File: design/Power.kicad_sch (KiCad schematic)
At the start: 43 parts, among them J5 PH_A, J6 PH_B, J7 PH_C, J8 SUPPLY, J9 GND, Q1 IRF7854, Q2 IRF7854, Q3 IRF7854, Q4 IRF7854, Q5 IRF7854, Q6 IRF7854, U5 AD8418, U6 AD8418, U7 AD8418

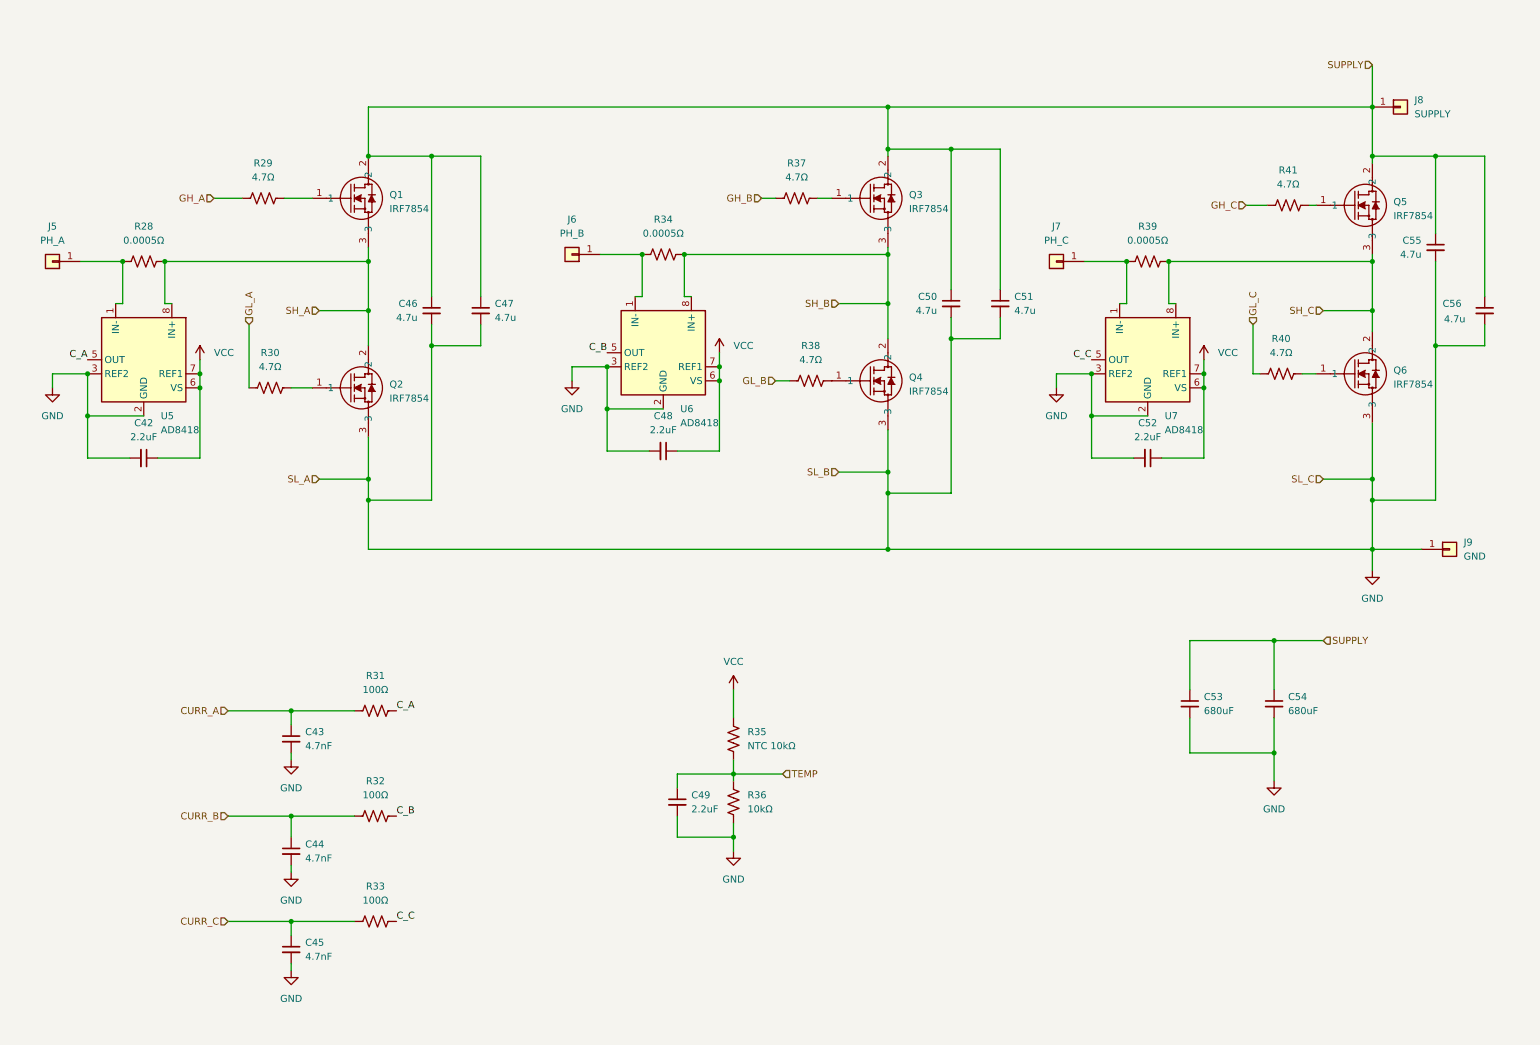
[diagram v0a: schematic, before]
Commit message: Ordenado del esquemático
- Cambios en los capacitores del oscilador
- Mejora de los esquemáticos, encapsulado la interfáz usb y los sensores del motor
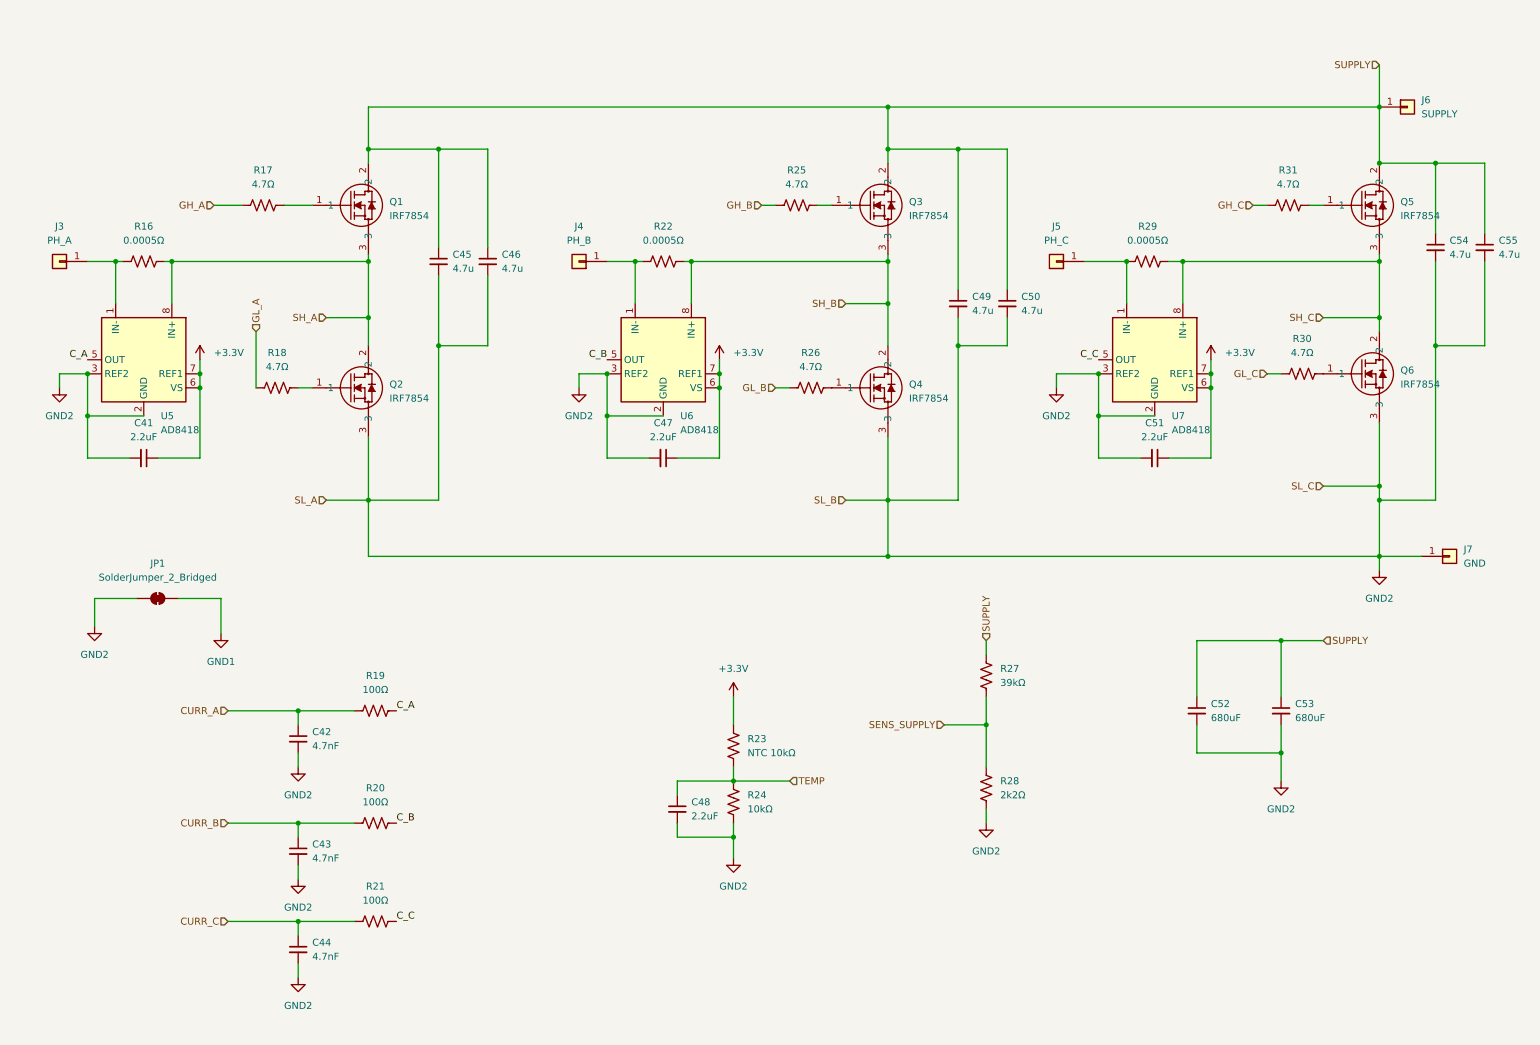
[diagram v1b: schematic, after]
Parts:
- added JP1: SolderJumper_2_Bridged, symbol Jumper:SolderJumper_2_Bridged
- added R27: 39kΩ, Resistor_SMD:R_0603_1608Metric, symbol Device:R_US
- added R28: 2k2Ω, Resistor_SMD:R_0603_1608Metric, symbol Device:R_US
- renumbered C42 to C41, C43 to C42, C44 to C43, C45 to C44, C46 to C45, C47 to C46, C48 to C47, C49 to C48, C50 to C49, C51 to C50, C52 to C51, C53 to C52, C54 to C53, C55 to C54, C56 to C55, J5 to J3, J6 to J4, J7 to J5, J8 to J6, J9 to J7, R28 to R16, R29 to R17, R30 to R18, R31 to R19, R32 to R20, R33 to R21, R34 to R22, R35 to R23, R36 to R24, R37 to R25, R38 to R26, R39 to R29, R40 to R30, R41 to R31
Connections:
- net SUPPLY: now also R27.1
- net GND renamed GND2
- net GND2: now also JP1.1 (A), R28.1
- net VCC renamed +3.3V
- new net GND1: JP1.2 (B)
- new net SENS_SUPPLY: R27.2, R28.2
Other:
- moved on the sheet: C42, C43, C44, C45, C46, C47, C48, C49, C50, C51, C52, C53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

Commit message: Pequeños cambios
Pequeños cambios, eliminado de carpeta BLDC
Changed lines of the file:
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@@
 	(hierarchical_label "SUPPLY"
 		(shape input)
-		(at 259.08 20.32 180)
+		(at 259.08 20.32 90)
 		(fields_autoplaced yes)
 		(effects
@@
 				(size 1.27 1.27)
 			)
-			(justify right)
+			(justify left)
 		)
 	)

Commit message: Pequeños cambios
Pequeños cambios en esquemático
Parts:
- renumbered R16 to R17, R17 to R18, R18 to R19, R19 to R20, R20 to R21, R21 to R22, R22 to R23, R23 to R24, R24 to R25, R25 to R26, R26 to R27, R27 to R28, R28 to R29, R29 to R30, R30 to R32
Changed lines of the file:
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@@
 		(dnp no)
 		(fields_autoplaced yes)
-		(property "Reference" "R25"
+		(property "Reference" "R26"
 			(at 153.67 39.37 90)
 			(effects
@@
 			(project "ESCX"
 				(path "/6389d757-a1bd-4c0a-9d55-6114b19cc67a/00000000-0000-0000-0000-00005ae14a7c"
-					(reference "R25")
+					(reference "R26")
 					(unit 1)
 				)
@@
 		(dnp no)
 		(fields_autoplaced yes)
-		(property "Reference" "R22"
+		(property "Reference" "R23"
 			(at 129.54 49.53 90)
 			(effects
@@
 			(project "ESCX"
 				(path "/6389d757-a1bd-4c0a-9d55-6114b19cc67a/00000000-0000-0000-0000-00005ae14a7c"
-					(reference "R22")
+					(reference "R23")
 					(unit 1)
 				)
@@
 		(dnp no)
 		(fields_autoplaced yes)
-		(property "Reference" "R26"
+		(property "Reference" "R27"
 			(at 156.21 72.39 90)
 			(effects
@@
 			(project "ESCX"
 				(path "/6389d757-a1bd-4c0a-9d55-6114b19cc67a/00000000-0000-0000-0000-00005ae14a7c"
-					(reference "R26")
+					(reference "R27")
 					(unit 1)
 				)
@@
 		(dnp no)
 		(fields_autoplaced yes)
-		(property "Reference" "#PWR056"
+		(property "Reference" "#PWR058"
 			(at 139.7 77.47 0)
 			(effects
@@
 			(project "ESCX"
 				(path "/6389d757-a1bd-4c0a-9d55-6114b19cc67a/00000000-0000-0000-0000-00005ae14a7c"
-					(reference "#PWR056")
+					(reference "#PWR058")
 					(unit 1)
 				)
@@
 		(dnp no)
 		(fields_autoplaced yes)
-		(property "Reference" "R17"
+		(property "Reference" "R18"
 			(at 57.15 39.37 90)
 			(effects
@@
 			(project "ESCX"
 				(path "/6389d757-a1bd-4c0a-9d55-6114b19cc67a/00000000-0000-0000-0000-00005ae14a7c"
-					(reference "R17")
+					(reference "R18")
 					(unit 1)
 				)
@@
 		(dnp no)
 		(fields_autoplaced yes)
-		(property "Reference" "R16"
+		(property "Reference" "R17"
 			(at 35.56 49.53 90)
 			(effects
@@
 			(project "ESCX"
 				(path "/6389d757-a1bd-4c0a-9d55-6114b19cc67a/00000000-0000-0000-0000-00005ae14a7c"
-					(reference "R16")
+					(reference "R17")
 					(unit 1)
 				)
@@
 		(dnp no)
 		(fields_autoplaced yes)
-		(property "Reference" "R18"
+		(property "Reference" "R19"
 			(at 59.69 72.39 90)
 			(effects
@@
 			(project "ESCX"
 				(path "/6389d757-a1bd-4c0a-9d55-6114b19cc67a/00000000-0000-0000-0000-00005ae14a7c"
-					(reference "R18")
+					(reference "R19")
 					(unit 1)
 				)
@@
 		(dnp no)
 		(fields_autoplaced yes)
-		(property "Reference" "#PWR051"
+		(property "Reference" "#PWR052"
 			(at 45.72 77.47 0)
 			(effects
@@
 			(project "ESCX"
 				(path "/6389d757-a1bd-4c0a-9d55-6114b19cc67a/00000000-0000-0000-0000-00005ae14a7c"
-					(reference "#PWR051")
+					(reference "#PWR052")
 					(unit 1)
 				)
@@
 		(dnp no)
 		(fields_autoplaced yes)
-		(property "Reference" "R29"
+		(property "Reference" "R30"
 			(at 217.17 49.53 90)
 			(effects
@@
 			(project "ESCX"
 				(path "/6389d757-a1bd-4c0a-9d55-6114b19cc67a/00000000-0000-0000-0000-00005ae14a7c"
-					(reference "R29")
+					(reference "R30")
 					(unit 1)
 				)
@@
 		(dnp no)
 		(fields_autoplaced yes)
-		(property "Reference" "R30"
+		(property "Reference" "R32"
 			(at 245.11 69.85 90)
 			(effects
@@
 			(project "ESCX"
 				(path "/6389d757-a1bd-4c0a-9d55-6114b19cc67a/00000000-0000-0000-0000-00005ae14a7c"
-					(reference "R30")
+					(reference "R32")
 					(unit 1)
 				)
@@
 		(dnp no)
 		(fields_autoplaced yes)
-		(property "Reference" "#PWR061"
+		(property "Reference" "#PWR063"
 			(at 228.6 77.47 0)
 			(effects
@@
 			(project "ESCX"
 				(path "/6389d757-a1bd-4c0a-9d55-6114b19cc67a/00000000-0000-0000-0000-00005ae14a7c"
-					(reference "#PWR061")
+					(reference "#PWR063")
 					(unit 1)
 				)
@@
 		(dnp no)
 		(fields_autoplaced yes)
-		(property "Reference" "#PWR63"
+		(property "Reference" "#PWR065"
 			(at 259.08 118.11 0)
 			(effects
@@
 			(project "ESCX"
 				(path "/6389d757-a1bd-4c0a-9d55-6114b19cc67a/00000000-0000-0000-0000-00005ae14a7c"
-					(reference "#PWR63")
+					(reference "#PWR065")
 					(unit 1)
 				)
@@
 		(dnp no)
 		(fields_autoplaced yes)
-		(property "Reference" "R19"
+		(property "Reference" "R20"
 			(at 77.47 130.81 90)
 			(effects
@@
 			(project "ESCX"
 				(path "/6389d757-a1bd-4c0a-9d55-6114b19cc67a/00000000-0000-0000-0000-00005ae14a7c"
-					(reference "R19")
+					(reference "R20")
 					(unit 1)
 				)
@@
 		(dnp no)
 		(fields_autoplaced yes)
-		(property "Reference" "R20"
+		(property "Reference" "R21"
 			(at 77.47 151.13 90)
 			(effects
@@
 			(project "ESCX"
 				(path "/6389d757-a1bd-4c0a-9d55-6114b19cc67a/00000000-0000-0000-0000-00005ae14a7c"
-					(reference "R20")
+					(reference "R21")
 					(unit 1)
 				)
@@
 		(dnp no)
 		(fields_autoplaced yes)
-		(property "Reference" "R21"
+		(property "Reference" "R22"
 			(at 77.47 168.91 90)
 			(effects
@@
 			(project "ESCX"
 				(path "/6389d757-a1bd-4c0a-9d55-6114b19cc67a/00000000-0000-0000-0000-00005ae14a7c"
-					(reference "R21")
+					(reference "R22")
 					(unit 1)
 				)
@@
 		(dnp no)
 		(fields_autoplaced yes)
-		(property "Reference" "#PWR057"
+		(property "Reference" "#PWR059"
 			(at 142.24 138.43 0)
 			(effects
@@
 			(project "ESCX"
 				(path "/6389d757-a1bd-4c0a-9d55-6114b19cc67a/00000000-0000-0000-0000-00005ae14a7c"
-					(reference "#PWR057")
+					(reference "#PWR059")
 					(unit 1)
 				)
@@
 		(dnp no)
 		(fields_autoplaced yes)
-		(property "Reference" "R24"
+		(property "Reference" "R25"
 			(at 144.78 152.3999 0)
 			(effects
@@
 			(project "ESCX"
 				(path "/6389d757-a1bd-4c0a-9d55-6114b19cc67a/00000000-0000-0000-0000-00005ae14a7c"
-					(reference "R24")
+					(reference "R25")
 					(unit 1)
 				)
@@
 		(dnp no)
 		(fields_autoplaced yes)
-		(property "Reference" "R23"
+		(property "Reference" "R24"
 			(at 144.78 142.2399 0)
 			(effects
@@
 			(project "ESCX"
 				(path "/6389d757-a1bd-4c0a-9d55-6114b19cc67a/00000000-0000-0000-0000-00005ae14a7c"
-					(reference "R23")
+					(reference "R24")
 					(unit 1)
 				)
@@
 		(dnp no)
 		(fields_autoplaced yes)
-		(property "Reference" "#PWR060"
+		(property "Reference" "#PWR062"
 			(at 200.66 85.09 0)
 			(effects
@@
 			(project "ESCX"
 				(path "/6389d757-a1bd-4c0a-9d55-6114b19cc67a/00000000-0000-0000-0000-00005ae14a7c"
-					(reference "#PWR060")
+					(reference "#PWR062")
 					(unit 1)
 				)
@@
 		(dnp no)
 		(fields_autoplaced yes)
-		(property "Reference" "#PWR055"
+		(property "Reference" "#PWR057"
 			(at 114.3 85.09 0)
 			(effects
@@
 			(project "ESCX"
 				(path "/6389d757-a1bd-4c0a-9d55-6114b19cc67a/00000000-0000-0000-0000-00005ae14a7c"
-					(reference "#PWR055")
+					(reference "#PWR057")
 					(unit 1)
 				)
@@
 		(dnp no)
 		(fields_autoplaced yes)
-		(property "Reference" "R28"
+		(property "Reference" "R29"
 			(at 190.5 149.8599 0)
 			(effects
@@
 			(project "ESCX"
 				(path "/6389d757-a1bd-4c0a-9d55-6114b19cc67a/00000000-0000-0000-0000-00005ae14a7c"
-					(reference "R28")
+					(reference "R29")
 					(unit 1)
 				)
@@
 		(dnp no)
 		(fields_autoplaced yes)
-		(property "Reference" "#PWR059"
+		(property "Reference" "#PWR061"
 			(at 187.96 163.83 0)
 			(effects
@@
 			(project "ESCX"
 				(path "/6389d757-a1bd-4c0a-9d55-6114b19cc67a/00000000-0000-0000-0000-00005ae14a7c"
-					(reference "#PWR059")
+					(reference "#PWR061")
 					(unit 1)
 				)
@@
 		(dnp no)
 		(fields_autoplaced yes)
-		(property "Reference" "#PWR053"
+		(property "Reference" "#PWR055"
 			(at 63.5 173.99 0)
 			(effects
@@
 			(project "ESCX"
 				(path "/6389d757-a1bd-4c0a-9d55-6114b19cc67a/00000000-0000-0000-0000-00005ae14a7c"
-					(reference "#PWR053")
+					(reference "#PWR055")
 					(unit 1)
 				)
@@
 		(dnp no)
 		(fields_autoplaced yes)
-		(property "Reference" "#PWR052"
+		(property "Reference" "#PWR054"
 			(at 63.5 153.67 0)
 			(effects
@@
 			(project "ESCX"
 				(path "/6389d757-a1bd-4c0a-9d55-6114b19cc67a/00000000-0000-0000-0000-00005ae14a7c"
-					(reference "#PWR052")
+					(reference "#PWR054")
 					(unit 1)
 				)
@@
 		(dnp no)
 		(fields_autoplaced yes)
-		(property "Reference" "R27"
+		(property "Reference" "R28"
 			(at 190.5 129.5399 0)
 			(effects
@@
 			(project "ESCX"
 				(path "/6389d757-a1bd-4c0a-9d55-6114b19cc67a/00000000-0000-0000-0000-00005ae14a7c"
-					(reference "R27")
+					(reference "R28")
 					(unit 1)
 				)
@@
 		(dnp no)
 		(fields_autoplaced yes)
-		(property "Reference" "#PWR074"
+		(property "Reference" "#PWR051"
 			(at 26.67 128.27 0)
 			(effects
@@
 			(project "ESCX"
 				(path "/6389d757-a1bd-4c0a-9d55-6114b19cc67a/00000000-0000-0000-0000-00005ae14a7c"
-					(reference "#PWR074")
+					(reference "#PWR051")
 					(unit 1)
 				)
@@
 		(dnp no)
 		(fields_autoplaced yes)
-		(property "Reference" "#PWR058"
+		(property "Reference" "#PWR060"
 			(at 142.24 170.18 0)
 			(effects
@@
 			(project "ESCX"
 				(path "/6389d757-a1bd-4c0a-9d55-6114b19cc67a/00000000-0000-0000-0000-00005ae14a7c"
-					(reference "#PWR058")
+					(reference "#PWR060")
 					(unit 1)
 				)
@@
 		(dnp no)
 		(fields_autoplaced yes)
-		(property "Reference" "#PWR054"
+		(property "Reference" "#PWR056"
 			(at 63.5 191.77 0)
 			(effects
@@
 			(project "ESCX"
 				(path "/6389d757-a1bd-4c0a-9d55-6114b19cc67a/00000000-0000-0000-0000-00005ae14a7c"
-					(reference "#PWR054")
+					(reference "#PWR056")
 					(unit 1)
 				)
@@
 		(dnp no)
 		(fields_autoplaced yes)
-		(property "Reference" "#PWR062"
+		(property "Reference" "#PWR064"
 			(at 241.3 156.21 0)
 			(effects
@@
 			(project "ESCX"
 				(path "/6389d757-a1bd-4c0a-9d55-6114b19cc67a/00000000-0000-0000-0000-00005ae14a7c"
-					(reference "#PWR062")
+					(reference "#PWR064")
 					(unit 1)
 				)
@@
 		(dnp no)
 		(fields_autoplaced yes)
-		(property "Reference" "#PWR075"
+		(property "Reference" "#PWR053"
 			(at 49.53 129.54 0)
 			(effects
@@
 			(project "ESCX"
 				(path "/6389d757-a1bd-4c0a-9d55-6114b19cc67a/00000000-0000-0000-0000-00005ae14a7c"
-					(reference "#PWR075")
+					(reference "#PWR053")
 					(unit 1)
 				)

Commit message: Agrego MFR# de conectores
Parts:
- removed J3: PH_A, symbol Connector_Generic:Conn_01x01
- removed J4: PH_B, symbol Connector_Generic:Conn_01x01
- removed J5: PH_C, symbol Connector_Generic:Conn_01x01
- removed J6: SUPPLY, symbol Connector_Generic:Conn_01x01
- removed J7: GND, symbol Connector_Generic:Conn_01x01
- added J10: Screw_Terminal_01x03, TerminalBlock_Phoenix:TerminalBlock_Phoenix_MKDS-1,5-3-5.08_1x03_P5.08mm_Horizontal, symbol Connector:Screw_Terminal_01x03
- added J11: Screw_Terminal_01x02, TerminalBlock_Phoenix:TerminalBlock_Phoenix_MKDS-1,5-2-5.08_1x02_P5.08mm_Horizontal, symbol Connector:Screw_Terminal_01x02
- JP1: footprint (none) -> Connector_PinHeader_2.54mm:PinHeader_1x02_P2.54mm_Vertical
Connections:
- net GND2: now also J11.2 (Pin_2)
- net SUPPLY: now also J11.1 (Pin_1)
- net PH_B: now reaches R23.2, U6.1 (IN-)
- net PH_B: now also J10.2 (Pin_2)
- net PH_A: now reaches R17.2, U5.1 (IN-)
- net PH_A: now also J10.1 (Pin_1)
- net PH_C: now reaches R30.2, U7.1 (IN-)
- net PH_C: now also J10.3 (Pin_3)
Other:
- moved on the sheet: C42, C43, C44, C48, C52, C53, JP1, R20, R21, R22, R24, R25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

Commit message: Ruteo del driver y ubicacion de MOSFETs
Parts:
- Q1, Q2, Q3, Q4, Q5, Q6: footprint SO-8_INF -> crf1:SO-8_INF_IRF7854
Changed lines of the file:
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@@
 			)
 		)
-		(property "Footprint" "SO-8_INF"
+		(property "Footprint" "crf1:SO-8_INF_IRF7854"
 			(at 61.722 39.878 0)
 			(effects
@@
 			)
 		)
-		(property "Footprint" "SO-8_INF"
+		(property "Footprint" "crf1:SO-8_INF_IRF7854"
 			(at 61.722 72.898 0)
 			(effects
@@
 			)
 		)
-		(property "Footprint" "SO-8_INF"
+		(property "Footprint" "crf1:SO-8_INF_IRF7854"
 			(at 155.702 39.878 0)
 			(effects
@@
 			)
 		)
-		(property "Footprint" "SO-8_INF"
+		(property "Footprint" "crf1:SO-8_INF_IRF7854"
 			(at 155.702 72.898 0)
 			(effects
@@
 			)
 		)
-		(property "Footprint" "SO-8_INF"
+		(property "Footprint" "crf1:SO-8_INF_IRF7854"
 			(at 244.602 70.358 0)
 			(effects
@@
 			)
 		)
-		(property "Footprint" "SO-8_INF"
+		(property "Footprint" "crf1:SO-8_INF_IRF7854"
 			(at 244.602 39.878 0)
 			(effects

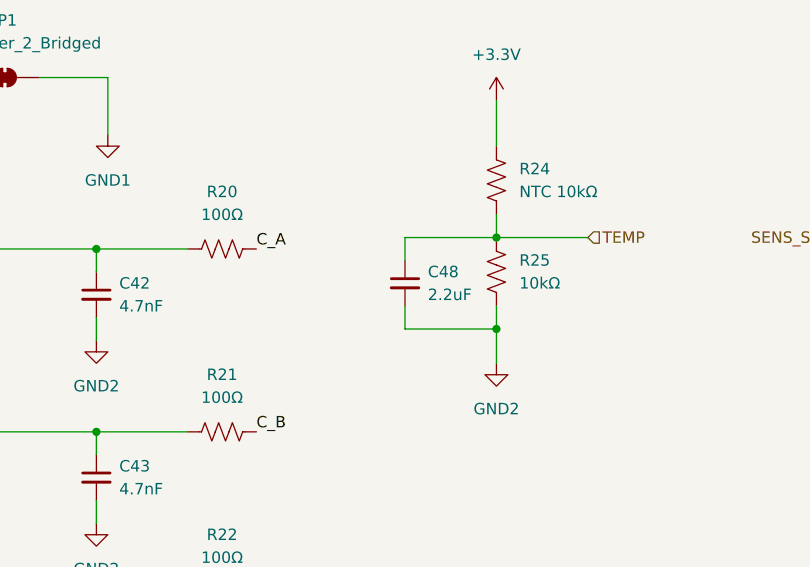
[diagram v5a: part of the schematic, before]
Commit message: Complete ruteo, menos plano GND2
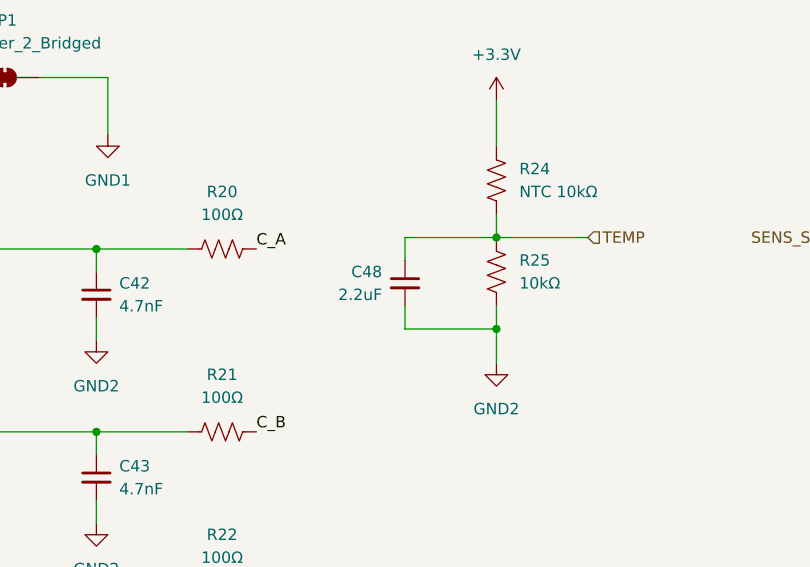
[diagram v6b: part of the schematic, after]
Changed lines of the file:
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@@
 		(lib_id "Device:C_Small")
 		(at 148.59 144.78 0)
+		(mirror y)
 		(unit 1)
 		(exclude_from_sim no)
@@
 		(on_board yes)
 		(dnp no)
-		(fields_autoplaced yes)
 		(property "Reference" "C48"
-			(at 151.13 143.5162 0)
+			(at 146.05 143.5162 0)
 			(effects
 				(font
@@
 		)
 		(property "Value" "2.2uF"
-			(at 151.13 146.0562 0)
+			(at 146.05 146.0562 0)
 			(effects
 				(font
